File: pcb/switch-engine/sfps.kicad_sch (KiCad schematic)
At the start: 1 part, among them U8 XILINX_ULTRASCALEPLUS_B676

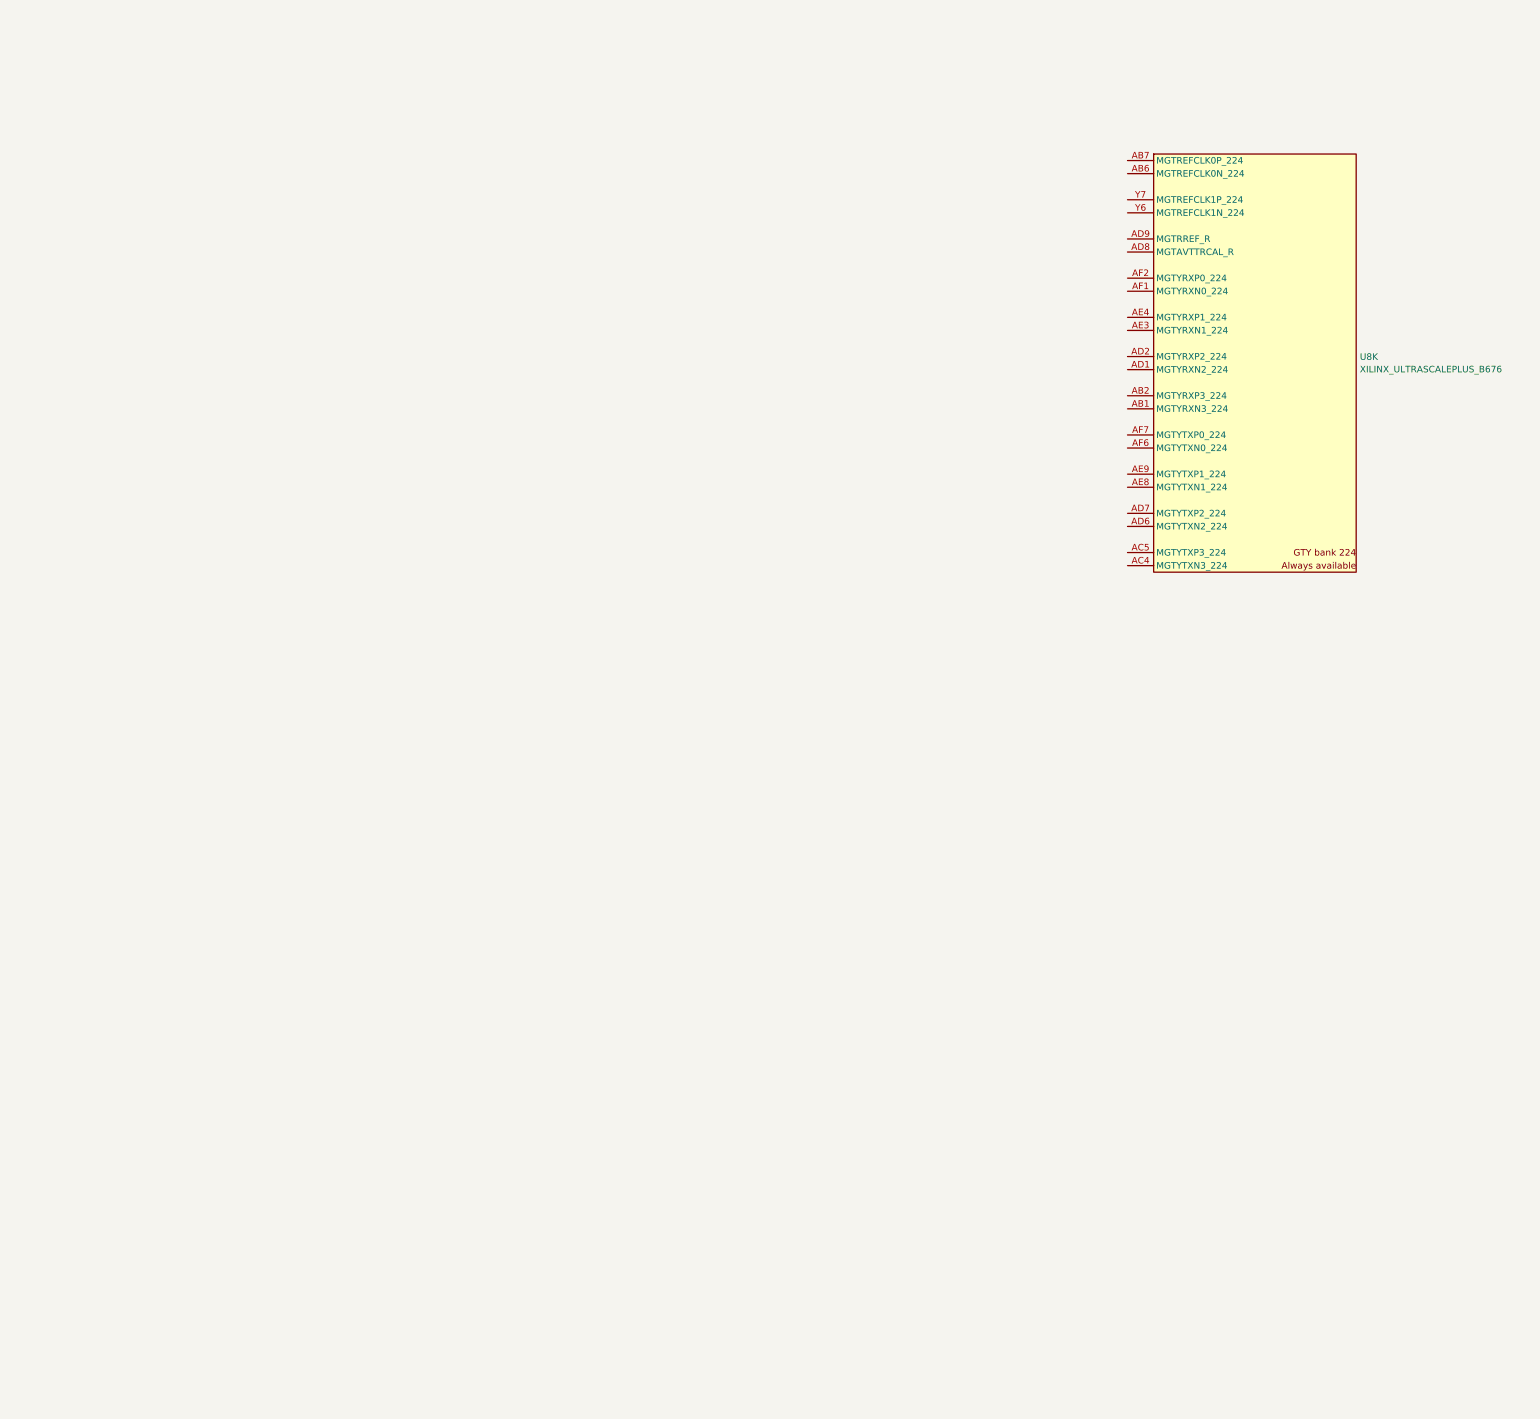
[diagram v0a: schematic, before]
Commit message: Continued initial schematic work on switch engine
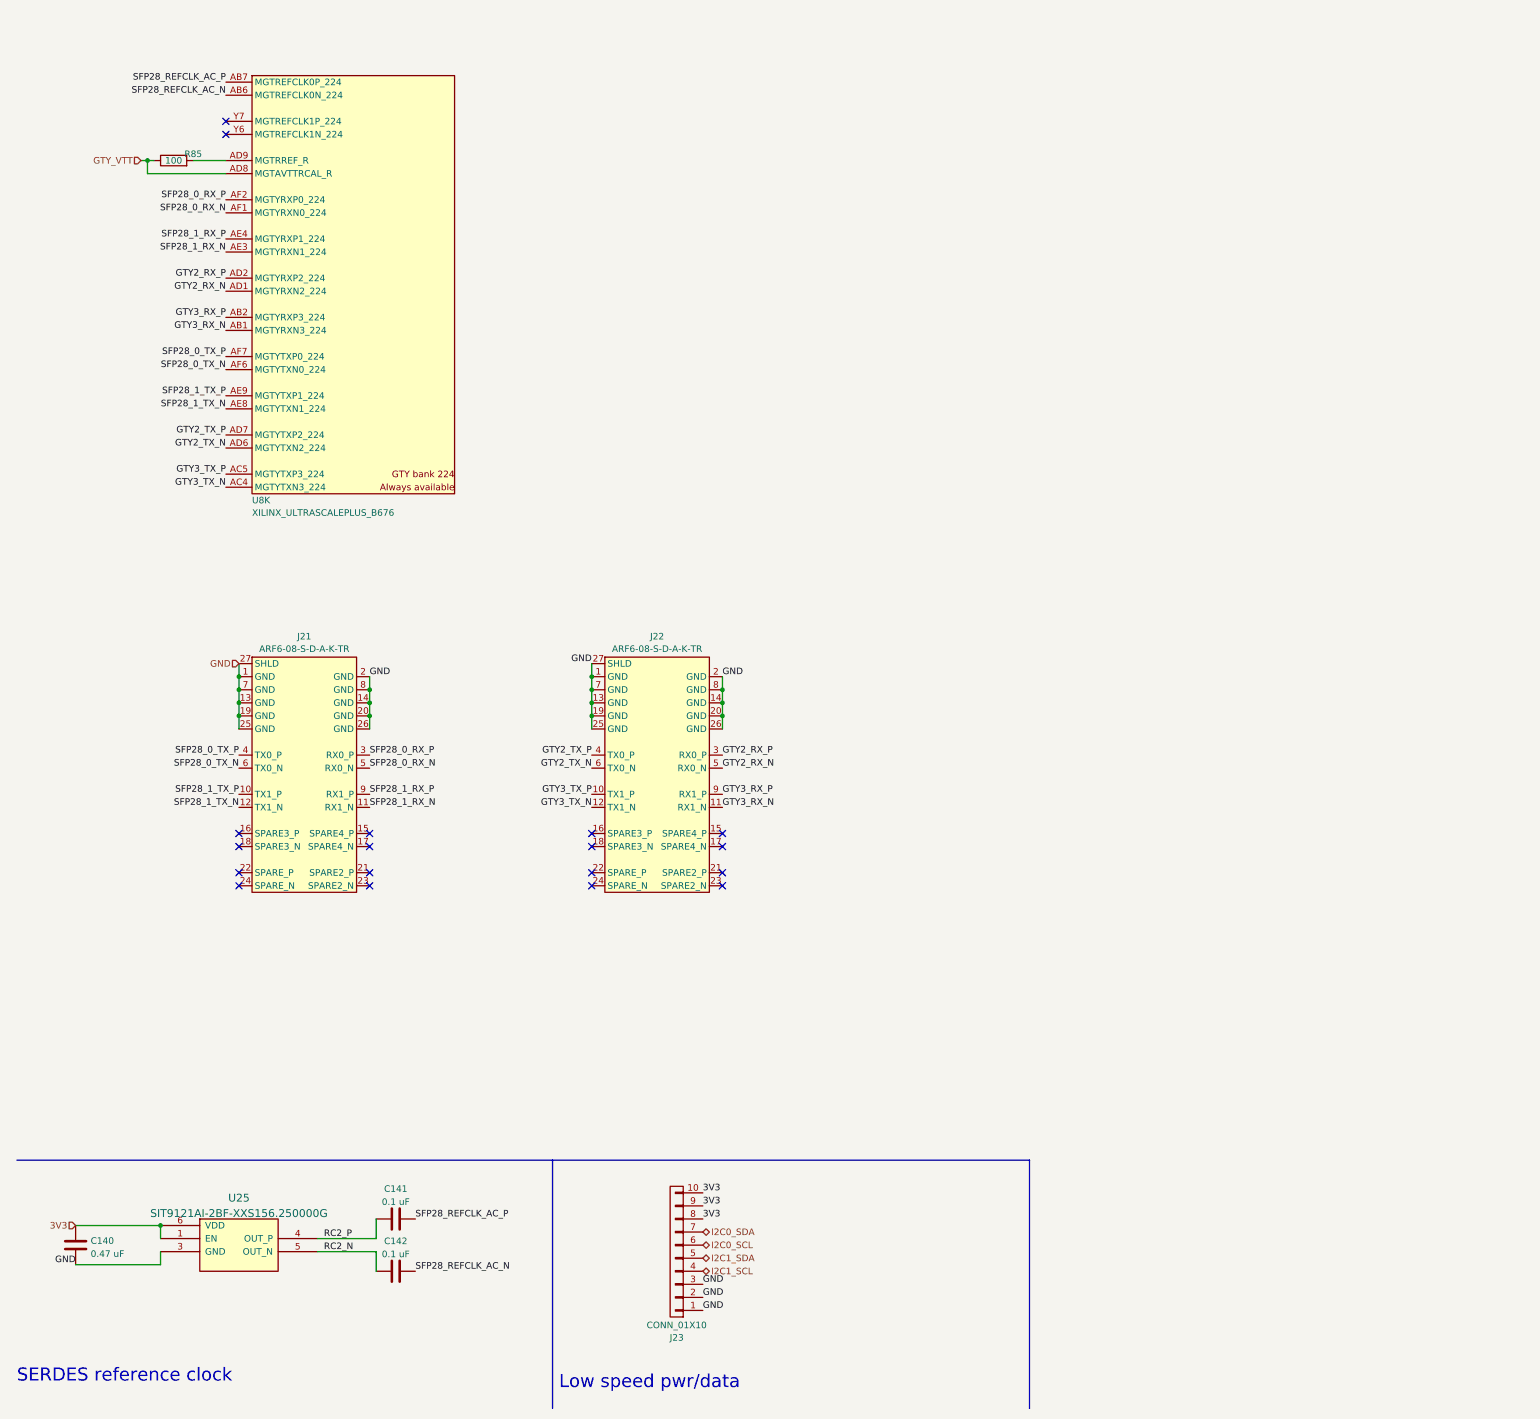
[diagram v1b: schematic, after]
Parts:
- added C140: 0.47 uF, azonenberg_pcb:EIA_0402_CAP_NOSILK, symbol device:C
- added C141, C142: 0.1 uF, azonenberg_pcb:EIA_0402_CAP_NOSILK, symbol device:C
- added J21, J22: ARF6-08-S-D-A-K-TR, azonenberg_pcb:CONN_SAMTEC_ARF6-08-S-D-A-K-TR, symbol special-azonenberg:CONN_LATENTRED_SFP28_HS_HOST
- added J23: CONN_01X10, azonenberg_pcb:CONN_MOLEX_PICOBLADE_10POS_0532611071, symbol conn:CONN_01X10
- added R85: 100, azonenberg_pcb:EIA_0402_RES_NOSILK, symbol device:R
- added U25: SIT9121AI-2BF-XXS156.250000G, azonenberg_pcb:OSCILLATOR_LVDS_3.2x2.5, symbol osc-azonenberg:OSC_LVDS_NOPAD
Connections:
- net GTY3_RX_N: now reaches U8.AB1 (MGTYRXN3_224)
- net GTY3_RX_N: now also J22.11 (RX1_N)
- net GTY3_RX_P: now reaches U8.AB2 (MGTYRXP3_224)
- net GTY3_RX_P: now also J22.9 (RX1_P)
- net SFP28_REFCLK_AC_N: now reaches U8.AB6 (MGTREFCLK0N_224)
- net SFP28_REFCLK_AC_N: now also C142.2
- net SFP28_REFCLK_AC_P: now reaches U8.AB7 (MGTREFCLK0P_224)
- net SFP28_REFCLK_AC_P: now also C141.2
- net GTY3_TX_N: now reaches U8.AC4 (MGTYTXN3_224)
- net GTY3_TX_N: now also J22.12 (TX1_N)
- net GTY3_TX_P: now reaches U8.AC5 (MGTYTXP3_224)
- net GTY3_TX_P: now also J22.10 (TX1_P)
- net GTY2_RX_N: now reaches U8.AD1 (MGTYRXN2_224)
- net GTY2_RX_N: now also J22.5 (RX0_N)
- net GTY2_RX_P: now reaches U8.AD2 (MGTYRXP2_224)
- net GTY2_RX_P: now also J22.3 (RX0_P)
- net GTY2_TX_N: now reaches U8.AD6 (MGTYTXN2_224)
- net GTY2_TX_N: now also J22.6 (TX0_N)
- net GTY2_TX_P: now reaches U8.AD7 (MGTYTXP2_224)
- net GTY2_TX_P: now also J22.4 (TX0_P)
- net GTY_VTT: now reaches U8.AD8 (MGTAVTTRCAL_R)
- net GTY_VTT: now also R85.1
- net at U8.AD9 (MGTRREF_R): now also R85.2
- net SFP28_1_RX_N: now reaches U8.AE3 (MGTYRXN1_224)
- net SFP28_1_RX_N: now also J21.11 (RX1_N)
- net SFP28_1_RX_P: now reaches U8.AE4 (MGTYRXP1_224)
- net SFP28_1_RX_P: now also J21.9 (RX1_P)
- net SFP28_1_TX_N: now reaches U8.AE8 (MGTYTXN1_224)
- net SFP28_1_TX_N: now also J21.12 (TX1_N)
- net SFP28_1_TX_P: now reaches U8.AE9 (MGTYTXP1_224)
- net SFP28_1_TX_P: now also J21.10 (TX1_P)
- net SFP28_0_RX_N: now reaches U8.AF1 (MGTYRXN0_224)
- net SFP28_0_RX_N: now also J21.5 (RX0_N)
- net SFP28_0_RX_P: now reaches U8.AF2 (MGTYRXP0_224)
- net SFP28_0_RX_P: now also J21.3 (RX0_P)
- net SFP28_0_TX_N: now reaches U8.AF6 (MGTYTXN0_224)
- net SFP28_0_TX_N: now also J21.6 (TX0_N)
- net SFP28_0_TX_P: now reaches U8.AF7 (MGTYTXP0_224)
- net SFP28_0_TX_P: now also J21.4 (TX0_P)
- new net 3V3: C140.1, J23.10 (P10), J23.8 (P8), J23.9 (P9), U25.1 (EN), U25.6 (VDD)
- new net GND: C140.2, J21.1 (GND), J21.13 (GND), J21.14 (GND), J21.19 (GND), J21.2 (GND), J21.20 (GND), J21.25 (GND), J21.26 (GND), J21.27 (SHLD), J21.7 (GND), J21.8 (GND), J22.1 (GND), J22.13 (GND), J22.14 (GND), J22.19 (GND), J22.2 (GND), J22.20 (GND), J22.25 (GND), J22.26 (GND), J22.27 (SHLD), J22.7 (GND), J22.8 (GND), J23.1 (P1), J23.2 (P2), J23.3 (P3), U25.3 (GND)
- new net I2C0_SCL: J23.6 (P6)
- new net I2C0_SDA: J23.7 (P7)
- new net I2C1_SCL: J23.4 (P4)
- new net I2C1_SDA: J23.5 (P5)
- new net RC2_N: C142.1, U25.5 (OUT_N)
- new net RC2_P: C141.1, U25.4 (OUT_P)
- no-connect marks 0 -> 18
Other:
- note added: "Low speed pwr/data"
- note added: "SERDES reference clock"
- moved on the sheet: U8K

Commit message: First iteration of main board PCB schematic is now passing ERC
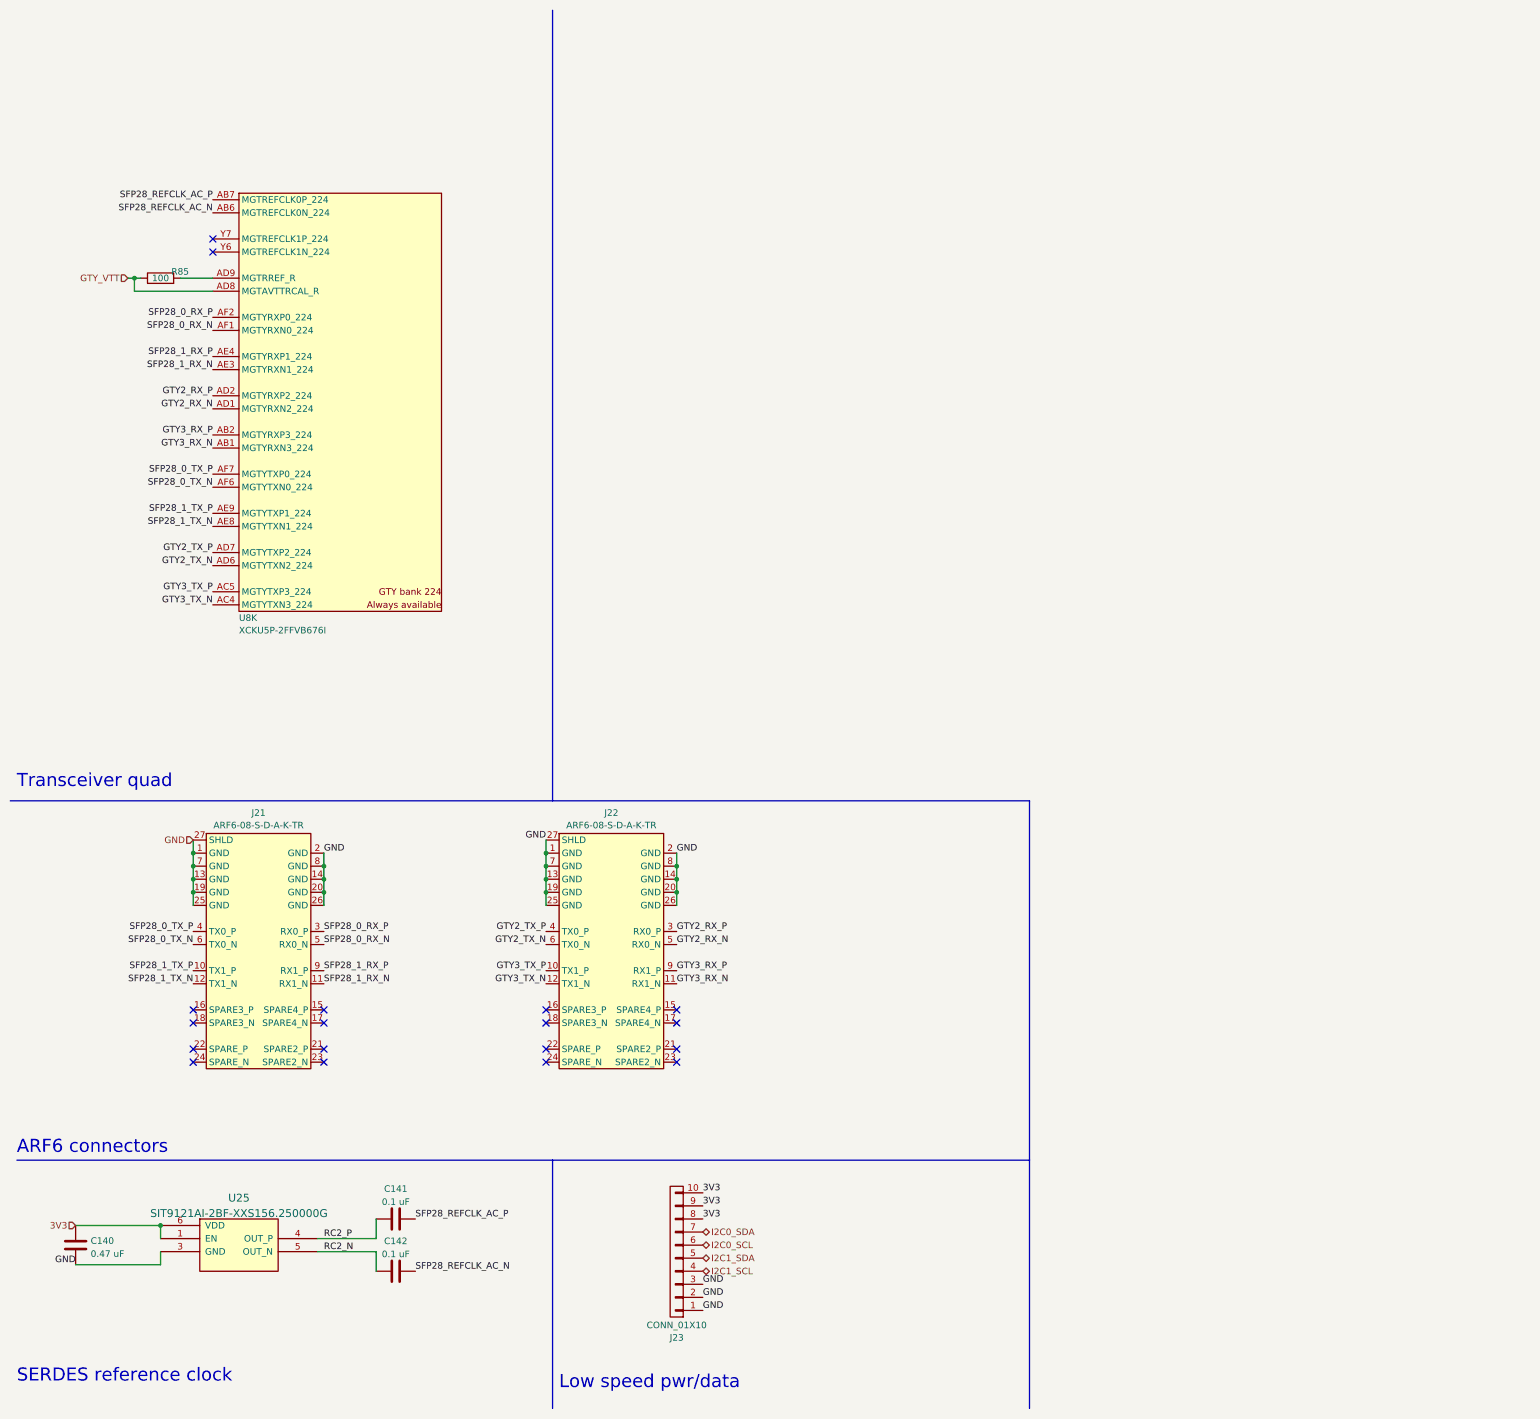
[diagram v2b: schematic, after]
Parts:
- U8: value XILINX_ULTRASCALEPLUS_B676 -> XCKU5P-2FFVB676I
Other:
- note added: "ARF6 connectors"
- note added: "Transceiver quad"
- company: (none) -> Antikernel Labs
- title: (none) -> LATENTRED Ethernet Switch - Main Board
- moved on the sheet: J21, J22, R85, U8K

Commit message: Finished schematic review
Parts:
- added C156, C157: 0.1 uF, symbol device:C
- added J11, J24: SMPM, symbol conn:CONN_COAXIAL
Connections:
- net GND: now also J11.2 (Ext), J24.2 (Ext)
- net REFCLK_OUT_N: now reaches U8.Y6 (MGTREFCLK1N_224)
- net REFCLK_OUT_N: now also C157.1
- net REFCLK_OUT_P: now reaches U8.Y7 (MGTREFCLK1P_224)
- net REFCLK_OUT_P: now also C156.1
- new net REFO_N: C157.2, J24.1 (In)
- new net REFO_P: C156.2, J11.1 (In)
- no-connect marks 18 -> 16
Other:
- note added: "Recovered clock out"

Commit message: Added footprints and created initial skeleton of layout
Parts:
- C156, C157: footprint (none) -> azonenberg_pcb:EIA_0402_CAP_NOSILK
- J11, J24: footprint (none) -> azonenberg_pcb:CONN_SMPM_AMPHENOL_C925-197J-51PT
- U8: footprint (none) -> azonenberg_pcb:BGA_676_27x27_FULLARRAY_1MM_FFG676
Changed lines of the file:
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@@
 			)
 		)
-		(property "Footprint" ""
+		(property "Footprint" "azonenberg_pcb:EIA_0402_CAP_NOSILK"
 			(at 248.92 256.8448 0)
 			(effects
@@
 			)
 		)
-		(property "Footprint" ""
+		(property "Footprint" "azonenberg_pcb:CONN_SMPM_AMPHENOL_C925-197J-51PT"
 			(at 261.62 257.81 0)
 			(effects
@@
 			)
 		)
-		(property "Footprint" ""
+		(property "Footprint" "azonenberg_pcb:BGA_676_27x27_FULLARRAY_1MM_FFG676"
 			(at 120.65 128.27 0)
 			(effects
@@
 			)
 		)
-		(property "Footprint" ""
+		(property "Footprint" "azonenberg_pcb:CONN_SMPM_AMPHENOL_C925-197J-51PT"
 			(at 261.62 247.65 0)
 			(effects
@@
 			)
 		)
-		(property "Footprint" ""
+		(property "Footprint" "azonenberg_pcb:EIA_0402_CAP_NOSILK"
 			(at 248.92 246.6848 0)
 			(effects

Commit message: Lots of progress routing ARC6s
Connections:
- net GTY2_RX_N: now also U8.AB2 (MGTYRXP3_224); no longer U8.AD1 (MGTYRXN2_224)
- net GTY2_RX_P: now also U8.AB1 (MGTYRXN3_224); no longer U8.AD2 (MGTYRXP2_224)
- net GTY2_TX_N: now also U8.AC4 (MGTYTXN3_224); no longer U8.AD6 (MGTYTXN2_224)
- net GTY2_TX_P: now also U8.AC5 (MGTYTXP3_224); no longer U8.AD7 (MGTYTXP2_224)
- net GTY3_RX_N: now also U8.AD2 (MGTYRXP2_224); no longer U8.AB1 (MGTYRXN3_224)
- net GTY3_RX_P: now also U8.AD1 (MGTYRXN2_224); no longer U8.AB2 (MGTYRXP3_224)
- net GTY3_TX_N: now also U8.AD6 (MGTYTXN2_224); no longer U8.AC4 (MGTYTXN3_224)
- net GTY3_TX_P: now also U8.AD7 (MGTYTXP2_224); no longer U8.AC5 (MGTYTXP3_224)
- net SFP28_0_RX_N: now also U8.AE3 (MGTYRXN1_224); no longer U8.AF1 (MGTYRXN0_224)
- net SFP28_0_RX_P: now also U8.AE4 (MGTYRXP1_224); no longer U8.AF2 (MGTYRXP0_224)
- net SFP28_0_TX_N: now also U8.AE8 (MGTYTXN1_224); no longer U8.AF6 (MGTYTXN0_224)
- net SFP28_0_TX_P: now also U8.AE9 (MGTYTXP1_224); no longer U8.AF7 (MGTYTXP0_224)
- net SFP28_1_RX_N: now also U8.AF1 (MGTYRXN0_224); no longer U8.AE3 (MGTYRXN1_224)
- net SFP28_1_RX_P: now also U8.AF2 (MGTYRXP0_224); no longer U8.AE4 (MGTYRXP1_224)
- net SFP28_1_TX_N: now also U8.AF6 (MGTYTXN0_224); no longer U8.AE8 (MGTYTXN1_224)
- net SFP28_1_TX_P: now also U8.AF7 (MGTYTXP0_224); no longer U8.AE9 (MGTYTXP1_224)
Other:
- note added: "Polarity swap"
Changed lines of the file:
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@@
+		)
+	)
+	(text "Polarity swap"
+		(exclude_from_sim no)
+		(at 22.86 87.63 0)
+		(effects
+			(font
+				(size 1.27 1.27)
+			)
+			(justify left)
+		)
+	)
+	(text "Polarity swap"
+		(exclude_from_sim no)
+		(at 22.86 95.25 0)
+		(effects
+			(font
+				(size 1.27 1.27)
+			)
+			(justify left)
 		)
 	)
@@
 	)
 	(label "SFP28_1_TX_N"
-		(at 52.07 113.03 180)
+		(at 52.07 105.41 180)
 		(fields_autoplaced yes)
 		(effects
@@
 	)
 	(label "GTY2_TX_N"
+		(at 52.07 128.27 180)
+		(fields_autoplaced yes)
+		(effects
+			(font
+				(size 1.27 1.27)
+			)
+			(justify right bottom)
+		)
+	)
+	(label "SFP28_1_TX_P"
+		(at 52.07 102.87 180)
+		(fields_autoplaced yes)
+		(effects
+			(font
+				(size 1.27 1.27)
+			)
+			(justify right bottom)
+		)
+	)
+	(label "GTY3_TX_N"
 		(at 52.07 120.65 180)
 		(fields_autoplaced yes)
@@
 		)
 	)
-	(label "SFP28_1_TX_P"
-		(at 52.07 110.49 180)
-		(fields_autoplaced yes)
-		(effects
-			(font
-				(size 1.27 1.27)
-			)
-			(justify right bottom)
-		)
-	)
-	(label "GTY3_TX_N"
-		(at 52.07 128.27 180)
-		(fields_autoplaced yes)
-		(effects
-			(font
-				(size 1.27 1.27)
-			)
-			(justify right bottom)
-		)
-	)
 	(label "GTY3_RX_P"
-		(at 52.07 95.25 180)
+		(at 52.07 90.17 180)
 		(fields_autoplaced yes)
 		(effects
@@
 	)
 	(label "SFP28_0_TX_N"
-		(at 52.07 105.41 180)
+		(at 52.07 113.03 180)
 		(fields_autoplaced yes)
 		(effects
@@
 	)
 	(label "GTY3_RX_N"
-		(at 52.07 97.79 180)
+		(at 52.07 87.63 180)
 		(fields_autoplaced yes)
 		(effects
@@
 	)
 	(label "SFP28_0_RX_N"
-		(at 52.07 74.93 180)
+		(at 52.07 82.55 180)
 		(fields_autoplaced yes)
 		(effects
@@
 	)
 	(label "GTY2_RX_P"
-		(at 52.07 87.63 180)
+		(at 52.07 97.79 180)
 		(fields_autoplaced yes)
 		(effects
@@
 	)
 	(label "GTY2_TX_P"
-		(at 52.07 118.11 180)
+		(at 52.07 125.73 180)
 		(fields_autoplaced yes)
 		(effects
@@
 	)
 	(label "GTY3_TX_P"
-		(at 52.07 125.73 180)
+		(at 52.07 118.11 180)
 		(fields_autoplaced yes)
 		(effects
@@
 	)
 	(label "SFP28_1_RX_P"
-		(at 52.07 80.01 180)
+		(at 52.07 72.39 180)
 		(fields_autoplaced yes)
 		(effects
@@
 	)
 	(label "SFP28_1_RX_N"
-		(at 52.07 82.55 180)
+		(at 52.07 74.93 180)
 		(fields_autoplaced yes)
 		(effects
@@
 	)
 	(label "GTY2_RX_N"
-		(at 52.07 90.17 180)
+		(at 52.07 95.25 180)
 		(fields_autoplaced yes)
 		(effects
@@
 	)
 	(label "SFP28_0_RX_P"
-		(at 52.07 72.39 180)
+		(at 52.07 80.01 180)
 		(fields_autoplaced yes)
 		(effects
@@
 	)
 	(label "SFP28_0_TX_P"
-		(at 52.07 102.87 180)
-		(fields_autoplaced yes)
-		(effects
+		(at 52.07 110.49 180)
+		(fields_autoplaced yes)
+		(effects
